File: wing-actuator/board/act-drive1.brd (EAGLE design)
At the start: 133.6 x 78.7 mm, 104 parts, among them J1 POWER_JACKPTH_LOCK, Q1 BSS123, Q2 BSS123, U5 Q50-5C, U7 LP2985-33, U8 TPS62160, X1 SMA-142-0701-801/806, X2 SMA-142-0701-801/806, X3 SMA-142-0701-801/806, X4 SMA-142-0701-801/806, X5 2516-

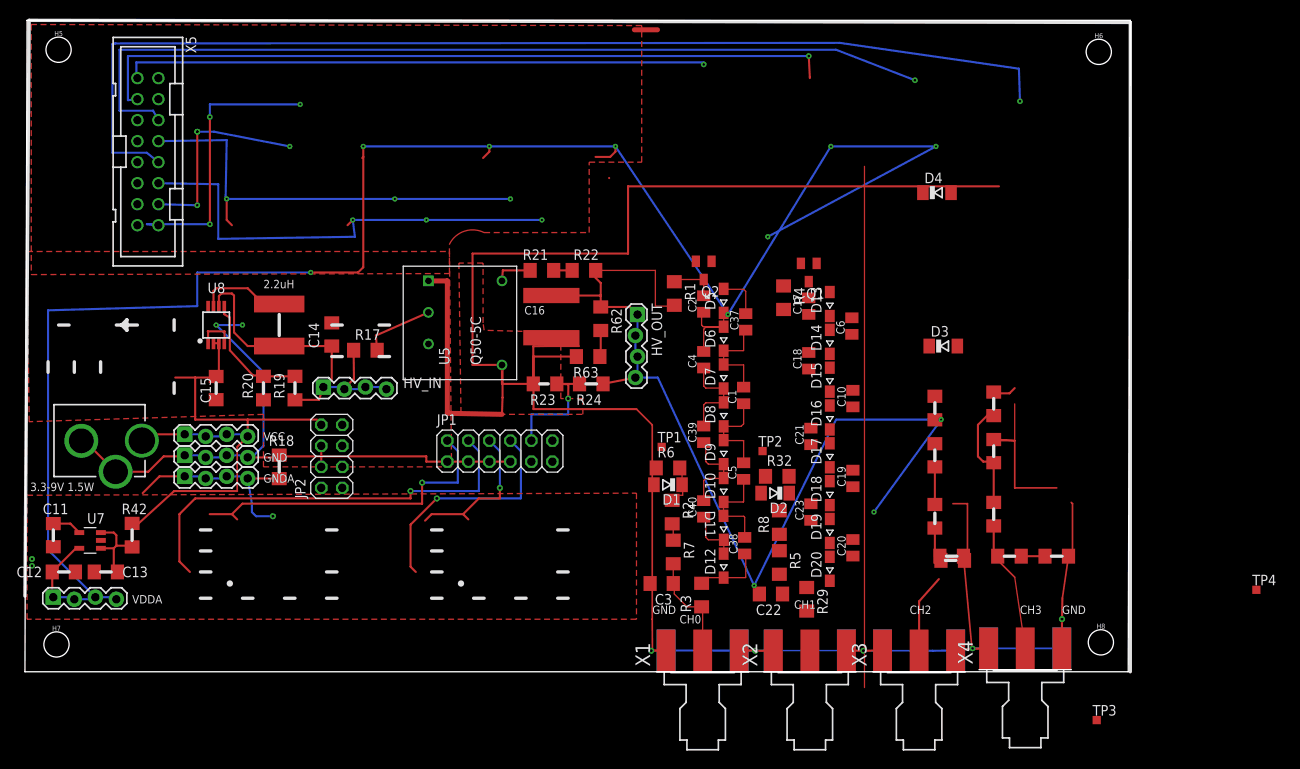
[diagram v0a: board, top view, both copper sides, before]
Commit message: updated library to include 1:10 xfmr
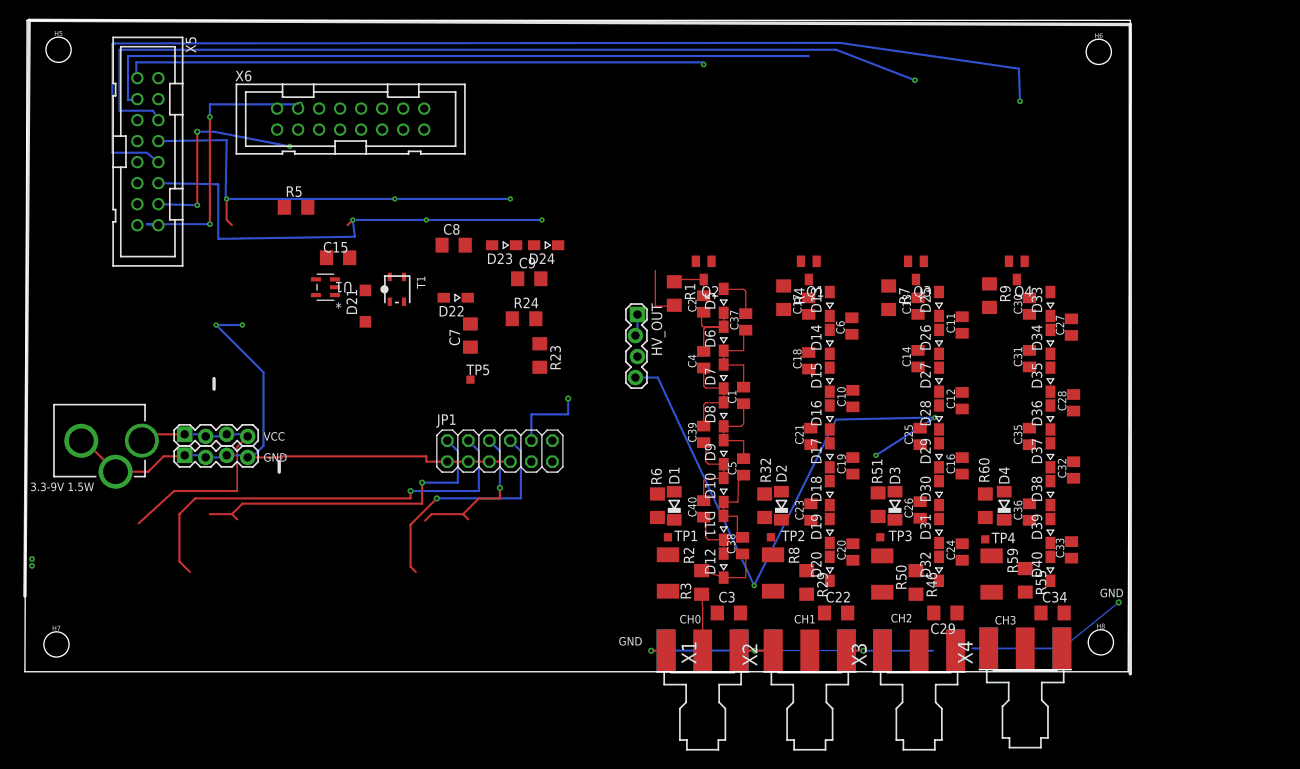
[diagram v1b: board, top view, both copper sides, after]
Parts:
- removed GNDA, HV_IN, VDDA: (no value), modular_robotics:1X04_LOCK
- removed JP2: (no value), pinhead:2X04
- removed L1: 2.2uH, modular_robotics:SRN6045
- removed R17: FUSE, rcl:R1206
- removed R18: 0R, rcl:R1206
- removed R19, R21, R22: 510k, rcl:R1206
- removed R20: 100k, rcl:R1206
- removed R42: FERRITE, rcl:R1206
- removed R47, R56: 5M, rcl:R1206
- removed R62, R63: 10M, rcl:R1206
- removed U5: Q50-5C, modular_robotics:Q50-5C
- removed U7: LP2985-33, modular_robotics:SOT23-5
- removed U8: TPS62160, modular_robotics:TSSOP8
- added C24, C25, C26, C27, C28, C30, C31, C32, C33, C35, C36: 3.3nF, rcl:C0805K
- added C7, C8, C9: 0.1uF 450V, rcl:C1206
- added D21: B0540W, diode:SOD123
- added D22, D23, D24, D25, D26, D27, D28, D29, D30, D31, D32, D33, D34, D35, D36, D37, D38, D39, D40: (no value), diode:SOD323-W
- added Q3, Q4: BSS123, transistor-small-signal:SOT23
- added R9: 10M, rcl:R1206
- added T1: ATB3225, lt3468-1:XFMR3225
- added TP5: TPTP10SQ, testpad:TP10SQ
- added U1: LT3468-1, ActuatorDrive:TSOT-23_S5
- added X6: 2516-, con-3m:PAK100/2500-16
- C11: value 10nF -> 3.3nF; device rcl:C1206 -> rcl:C0805K
- C12, C13: value 2.2uF -> 3.3nF; device rcl:C1206 -> rcl:C0805K
- C14: value 22uF -> 3.3nF; device rcl:C1206 -> rcl:C0805K
- C15: value 22uF -> 4.7uF
- C16: value 100nF-1k5V -> 3.3nF; device rcl:C2225K -> rcl:C0805K
- R2, R50, R59, R8: value 5M -> 10M; device rcl:R1206 -> rcl:R2010
- R24: value 100M -> 10M
- R5: value 5M -> 100K; device rcl:R1206 -> resistor:R1206
- R55: value 10M -> 1M
- R7: value 5M -> 10M
- moved C11 112.8 mm to (113.0, 41.9), turned to 90 degrees
- moved C12 110.5 mm to (113.0, 32.8), turned to 90 degrees
- moved C13 103.3 mm to (107.7, 44.2), turned to 90 degrees
- moved R5 72.5 mm to (32.5, 56.1), turned to 0 degrees
- moved C14 70.9 mm to (107.7, 37.8)
- moved C16 52.8 mm to (113.0, 24.9), turned to 90 degrees
- moved R7 40.3 mm to (104.1, 45.2)
- moved D4 38.7 mm to (118.1, 20.1), turned to 90 degrees
- moved TP3 34.2 mm to (103.1, 16.3)
- moved TP4 33.3 mm to (115.8, 16.0)
- moved R55 21.7 mm to (120.7, 11.0)
- moved C15 21.6 mm to (37.6, 50.0), turned to 180 degrees
- moved R46 21.2 mm to (107.4, 10.8)
- moved C34 20.8 mm to (124.0, 7.11), turned to 0 degrees
- moved D3 20.2 mm to (104.9, 20.1), turned to 90 degrees
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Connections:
- net SD_1 renamed START
- removed net GNDA: C11.2, C12.2, C13.2, GNDA.1, GNDA.2, GNDA.3, GNDA.4, R18.2, U7.2
- removed net ID0: D1.C, R2.1, R6.2, TP1.TP
- removed net ID1: D2.C, R32.2, R8.1, TP2.TP
- removed net ID2: D3.C, R50.1, R51.2, TP3.TP
- removed net ID3: D4.C, R59.1, R60.2, TP4.TP
- removed net I_SENSE_0: JP1.4
- removed net I_SENSE_1: JP1.8
- removed net N$60: R21.2, U5.3
- removed net N$62: R62.2, R63.1
- removed net SD_0: X5.1
- removed net VDDA: C12.1, U7.5, VDDA.1, VDDA.2, VDDA.3, VDDA.4
- removed net V_SENSE_0: JP1.2
- removed net V_SENSE_1: JP1.6
- new net +3V3: R5.2, X6.4, X6.8
- new net BOOST: C7.1, C8.2, D22.C, D23.C, D24.A, HV_OUT.4, R24.1
- new net DONE*: R5.1, U1.3, U1.4, X5.1
- new net N$28: X4.G@1, X4.G@2, X4.G@3, X4.G@4
- new net N$29: C25.1, C26.2, D29.C, D30.A
- new net N$30: C13.2, Q3.3, R7.1
- new net N$32: C30.1, C31.2, D33.C, D34.A
- new net N$33: C27.1, C28.2, D34.C, D35.A
- new net N$34: C36.1, D39.C, D40.A
- new net N$35: C28.1, C32.2, D36.C, D37.A
- new net N$36: C32.1, C33.2, D38.C, D39.A
- new net N$38: C35.1, C36.2, D37.C, D38.A
- new net N$39: C30.2, Q4.3, R9.1
- new net V_SENSE0: D1.C, JP1.2, R2.1, R6.2, TP1.TP
- new net V_SENSE1: D2.C, JP1.4, R32.2, R8.1, TP2.TP
- new net V_SENSE2: D3.C, JP1.6, R50.1, R51.2, TP3.TP
- new net V_SENSE3: D4.C, JP1.8, R59.1, R60.2, TP4.TP
- net GND: now also C11.2, C27.2, C7.2, C9.1, D21.A, D23.A, D25.A, D33.A, Q3.2, Q4.2, T1.S3, X6.12, X6.14; no longer C14.2, C16.2, JP2.4, JP2.6, R18.1, R20.1, R63.2, U5.1, U5.4, U8.1, U8.4, X3.G@1, X3.G@2, X3.G@3, X3.G@4, X4.G@1, X4.G@2, X4.G@3, X4.G@4
- net HV_SENSE: now also TP5.TP
- net N$12: now also D21.C, T1.P4; no longer R17.2, U5.2
- net N$17: now also C13.1, C14.2, D25.C, D26.A; no longer L1.1, U8.7
- net N$18: now also C11.1, C12.2, D26.C, D27.A; no longer C14.1, HV_IN.1, HV_IN.2, HV_IN.3, HV_IN.4, L1.2, R17.1, R19.1, U8.6
- net N$19: now also C9.2, D24.C; no longer C11.1, U7.4
- net N$20: now also C26.1, D31.C, D32.A; no longer R19.2, R20.2, U8.5
- net N$24: now also C12.1, C16.2, D28.C, D29.A; no longer R21.1, R22.1
- net N$25: now also C16.1, C24.2, D30.C, D31.A; no longer R47.2, R50.2
- net N$26: now also C33.1, D40.C
- net N$27: now also C14.1, C25.2, D27.C, D28.A; no longer R56.2, R59.2
- net N$37: now also C31.1, C35.2, D35.C, D36.A; no longer C13.1, R42.2, U7.1, U7.3
- net N$4: now also C24.1, D32.C, R46.1; no longer R2.2, R7.1
- net N$6: now also C8.1, D22.A, T1.S2; no longer R5.1, R8.2
- net PWM_2: now also Q3.1
- net PWM_3: now also Q4.1
- net V+: now also R7.2, R9.2; no longer C16.1, HV_OUT.2, HV_OUT.3, HV_OUT.4, R22.2, R24.1, R62.1
- net VCC: now also T1.P1, U1.6, X6.16; no longer JP2.8, R42.1, U8.2, U8.3
- net VO0: now also R2.2; no longer R7.2
- net VO1: now also R8.2; no longer R5.2, X2.1
- net VO2: now also R50.2; no longer R47.1
- net VO3: now also R59.2; no longer R56.1
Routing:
- net GND: track 420.6 -> 123.7 mm, vias 7 -> 5
- net VDDA: track 229.3 -> 0.00 mm, vias 8 -> 0
- net V+: track 120.6 -> 10.2 mm, vias 3 -> 0
- net BOOST: track 0.00 -> 73.6 mm, vias 0 -> 3
- net SD_0: track 71.0 -> 0.00 mm, vias 1 -> 0
- net DONE*: track 0.00 -> 71.0 mm, vias 0 -> 1
- net V_SENSE1: track 0.00 -> 52.0 mm, vias 0 -> 1
- net I_SENSE_0: track 52.0 -> 0.00 mm, vias 1 -> 0
- net N$18: track 48.1 -> 0.00 mm
- net N$28: track 63.0 -> 19.6 mm, vias 0 -> 1
- net V_SENSE_0: track 39.6 -> 0.00 mm, vias 1 -> 0
- net V_SENSE0: track 0.00 -> 39.6 mm, vias 0 -> 1
- net VCC: track 67.3 -> 34.0 mm
- net V_SENSE3: track 0.00 -> 28.1 mm, vias 0 -> 1
- net I_SENSE_1: track 28.1 -> 0.00 mm, vias 1 -> 0
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- removed copper zone on layer 1, net GND
- removed copper zone on layer 1, net GNDA
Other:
- board text removed: "2.2uH"

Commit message: placing flash boost converter
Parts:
- added C41, C42, C43, C44, C45, C46: 3.3nF, rcl:C0805K
- added Q5, Q6: BSS123, transistor-small-signal:SOT23
- added TP6, TP7: TPTP20SQ, testpad:TP20SQ
- added X7: SSW-102-02-S-D, con-samtec:SSW-102-02-S-D
- TP5: value TPTP10SQ -> TPTP20SQ; device testpad:TP10SQ -> testpad:TP20SQ
- moved TP5 71.5 mm to (121.2, 58.7)
- moved R24 60.4 mm to (117.9, 60.3), turned to 270 degrees
- moved R23 58.3 mm to (117.9, 55.0)
- moved C15 56.4 mm to (90.9, 68.3)
- moved R5 56.4 mm to (85.9, 74.4)
- moved U1 56.4 mm to (89.4, 64.8)
- moved D21 56.4 mm to (94.2, 62.5)
- moved T1 56.4 mm to (98.0, 64.5)
- moved C8 54.3 mm to (103.6, 67.1)
- moved C7 54.2 mm to (104.1, 60.2), turned to 270 degrees
- moved C9 53.7 mm to (110.2, 68.3), turned to 270 degrees
- moved D22 53.5 mm to (102.1, 63.5), turned to 90 degrees
- moved D23 53.0 mm to (108.0, 68.3), turned to 90 degrees
- moved D24 45.9 mm to (106.7, 64.8)
- moved HV_OUT 44.6 mm to (112.8, 64.5), turned to 0 degrees
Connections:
- removed net N$19: C9.2, D24.C
- removed net N$28: X4.G@1, X4.G@2, X4.G@3, X4.G@4
- new net BOOST1: C7.1, D22.C, X7.3
- new net BOOST2: C9.2, D24.C, X7.1
- new net N$40: C41.1, TP6.TP
- new net N$41: C41.2, C42.1
- new net N$42: C42.2, C43.1, Q5.3
- new net N$43: C44.1, TP7.TP
- new net N$44: C44.2, C45.1
- new net N$45: C45.2, C46.1, Q6.3
- net BOOST: no longer C7.1, D22.C, HV_OUT.4, R24.1
- net DONE*: no longer U1.4
- net GND: now also C43.2, C46.2, Q5.2, Q6.2, U1.2, X3.G@1, X3.G@2, X3.G@3, X3.G@4, X4.G@1, X4.G@2, X4.G@3, X4.G@4
- net N$12: now also U1.1
- net SD_2: now also Q5.1
- net SD_3: now also Q6.1
- net START: now also U1.4
- net V+: now also HV_OUT.2, HV_OUT.3, HV_OUT.4, R24.1, X7.2, X7.4
- net VO1: now also X2.1
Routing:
- net SD_3: track 132.8 -> 0.00 mm, vias 1 -> 0
- net SD_2: track 109.6 -> 0.00 mm, vias 1 -> 0
- net START: track 88.8 -> 0.00 mm
- net BOOST: track 73.6 -> 0.00 mm, vias 3 -> 0
- net DONE*: track 71.0 -> 0.18 mm, vias 1 -> 0
- net PWM_3: track 56.3 -> 0.90 mm, vias 3 -> 0
- net PWM_2: track 53.1 -> 3.44 mm, vias 3 -> 0
- net V_SENSE1: track 52.0 -> 14.9 mm, vias 1 -> 0
- net V_SENSE0: track 39.6 -> 9.92 mm, vias 1 -> 0
- net GND: track 123.7 -> 95.7 mm, vias 5 -> 4
- net PWM_1: track 34.4 -> 13.0 mm, vias 3 -> 0
- net VCC: track 34.0 -> 13.4 mm
- net N$28: track 19.6 -> 0.00 mm, vias 1 -> 0
- net PWM_0: track 24.9 -> 8.89 mm, vias 4 -> 0
- net V_SENSE2: track 18.6 -> 6.24 mm, vias 1 -> 0
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
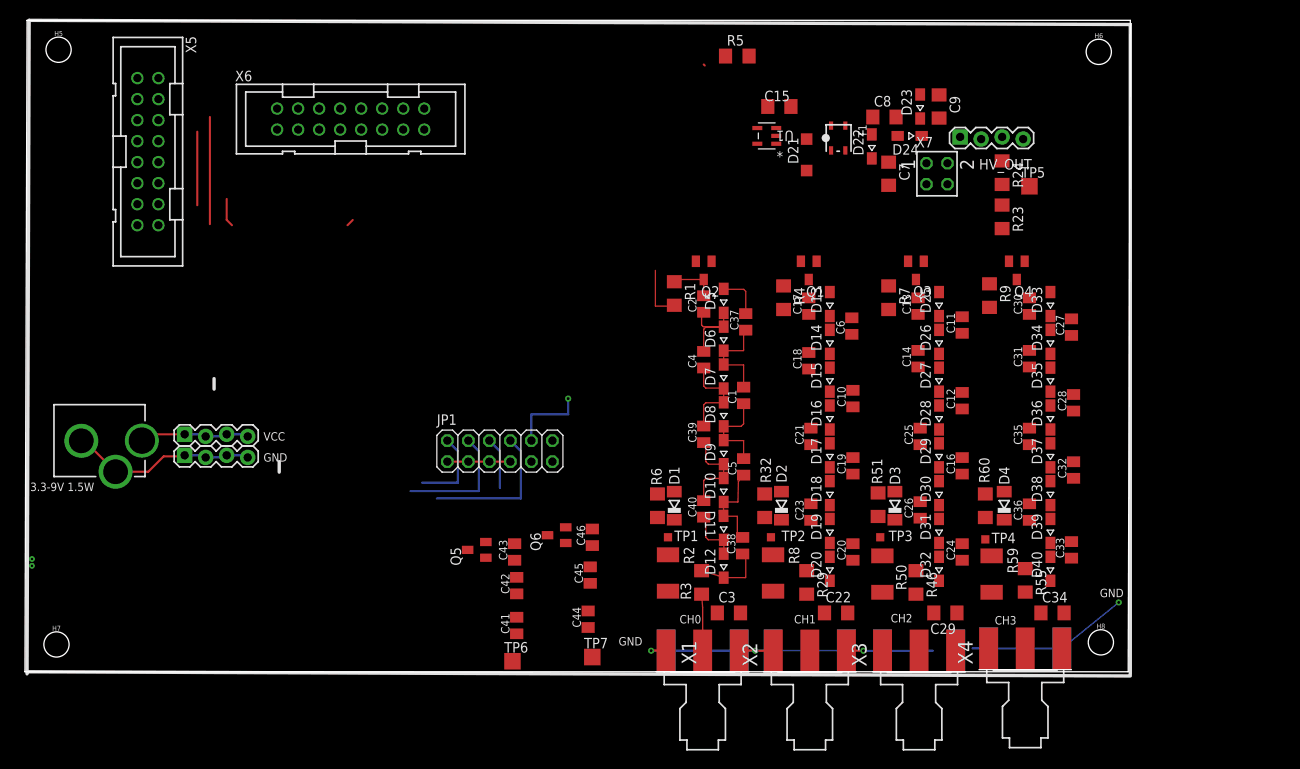
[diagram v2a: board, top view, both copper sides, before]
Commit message: started routing of wing actuator drive
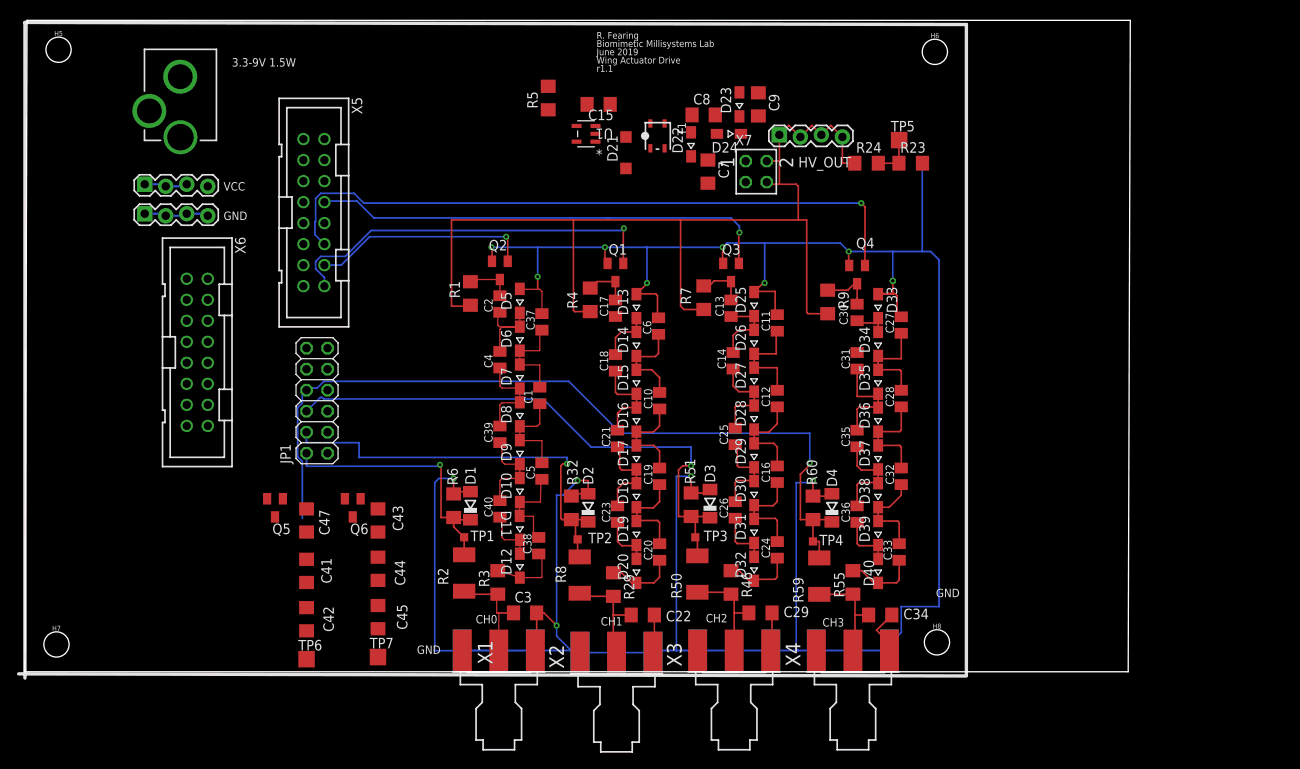
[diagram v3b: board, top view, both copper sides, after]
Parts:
- removed C46: 3.3nF, rcl:C0805K
- added C47: 220 pF, 1000V, rcl:C1206
- C41, C42, C43, C44, C45: value 3.3nF -> 220 pF, 1000V; device rcl:C0805K -> rcl:C1206
- moved J1 53.8 mm to (18.5, 78.5), turned to 180 degrees
- moved X6 33.7 mm to (20.6, 38.6), turned to 270 degrees
- moved VCC 30.6 mm to (14.2, 58.8)
- moved GND 29.6 mm to (14.2, 55.2)
- moved C41 26.2 mm to (33.8, 12.2)
- moved C45 26.2 mm to (42.4, 6.60)
- moved C44 26.1 mm to (42.4, 12.4)
- moved TP7 25.9 mm to (42.4, 1.78)
- moved C42 25.7 mm to (33.8, 6.35)
- moved Q5 24.9 mm to (30.0, 19.8), turned to 180 degrees
- moved TP6 24.9 mm to (33.8, 1.52)
- moved Q6 24.9 mm to (39.4, 19.8), turned to 180 degrees
- moved C1 24.6 mm to (62.0, 33.4)
- moved R3 24.6 mm to (56.9, 10.8)
- moved R6 24.6 mm to (51.6, 20.1)
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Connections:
- net GND: now also C47.2; no longer C46.2
- net N$40: now also C42.1; no longer C41.1
- net N$41: now also C41.1, C42.2; no longer C41.2, C42.1
- net N$42: now also C41.2, C47.1; no longer C42.2, C43.1
- net N$43: now also C45.1; no longer C44.1
- net N$44: now also C44.1, C45.2; no longer C44.2, C45.1
- net N$45: now also C43.1, C44.2; no longer C45.2, C46.1
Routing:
- net GND: track 95.7 -> 371.4 mm, vias 4 -> 14
- net V+: track 6.65 -> 128.4 mm
- net V_SENSE3: track 17.7 -> 100.8 mm, vias 0 -> 1
- net PWM_3: track 0.90 -> 80.5 mm, vias 0 -> 1
- net V_SENSE2: track 6.24 -> 68.2 mm, vias 0 -> 1
- net PWM_2: track 3.44 -> 56.0 mm, vias 0 -> 1
- net V_SENSE1: track 14.9 -> 51.2 mm, vias 0 -> 1
- net PWM_1: track 13.0 -> 46.6 mm, vias 0 -> 1
- net V_SENSE0: track 9.92 -> 33.0 mm, vias 0 -> 1
- net PWM_0: track 8.89 -> 26.4 mm, vias 0 -> 1
- net VO1: track 0.00 -> 13.3 mm
- net N$24: track 0.00 -> 13.3 mm
- net VO2: track 0.00 -> 12.9 mm
- net N$33: track 0.00 -> 12.8 mm
- net N$35: track 0.00 -> 12.8 mm
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
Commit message: more routing and adding ground plane
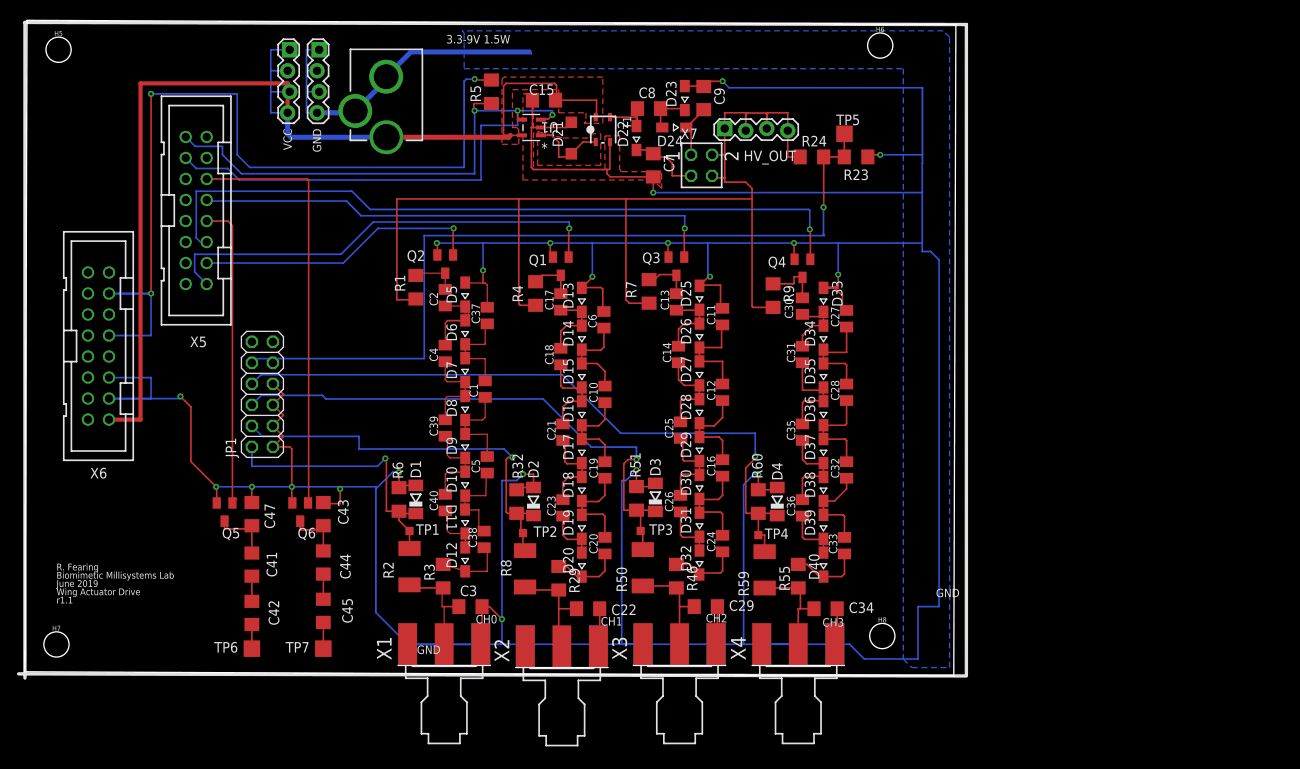
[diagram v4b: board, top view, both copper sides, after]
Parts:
- moved U$18 91.6 mm to (3.56, 8.26)
- moved GND 28.9 mm to (35.2, 75.2), turned to 270 degrees
- moved J1 24.9 mm to (43.4, 78.5)
- moved VCC 23.9 mm to (31.6, 75.2), turned to 270 degrees
- moved X5 14.2 mm to (20.4, 55.8)
- moved X6 12.0 mm to (8.64, 39.4)
- moved R5 6.90 mm to (56.1, 70.1)
- moved D21 6.84 mm to (65.8, 64.5)
- moved TP6 6.73 mm to (27.2, 2.79)
- moved TP7 6.68 mm to (35.8, 2.79)
- moved C7 6.65 mm to (75.7, 61.2)
- moved R8 6.65 mm to (60.2, 12.4)
- moved X1 6.65 mm to (50.4, 0.76)
- moved C10 6.65 mm to (69.8, 33.5)
- moved C11 6.65 mm to (84.1, 42.9)
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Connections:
- net SD_2: now also X5.10; no longer X5.6
- net SD_3: now also X5.6; no longer X5.10
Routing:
- net GND: track 371.4 -> 617.0 mm, vias 14 -> 21
- net VCC: track 6.40 -> 135.5 mm
- net +3V3: track 0.00 -> 104.2 mm, vias 0 -> 3
- net HV_SENSE: track 5.29 -> 99.4 mm, vias 0 -> 1
- net DONE*: track 0.00 -> 59.5 mm, vias 0 -> 2
- net SD_3: track 0.00 -> 51.4 mm
- net START: track 0.00 -> 51.2 mm, vias 0 -> 1
- net SD_2: track 0.00 -> 37.6 mm
- net V_SENSE3: track 100.8 -> 83.8 mm
- net V+: track 128.4 -> 143.5 mm
- net N$12: track 0.00 -> 9.50 mm
- net PWM_1: track 46.6 -> 55.4 mm
- net BOOST1: track 0.00 -> 8.79 mm
- net PWM_0: track 26.4 -> 34.9 mm
- net PWM_3: track 80.5 -> 88.4 mm
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- added copper zone on layer 1, net GND
- added copper zone on layer 16, net GND
- added copper zone on layer 1, net N$12
- added copper zone on layer 1, net VCC
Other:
- board size 133.6 x 78.7 mm -> 112.5 x 79.2 mm
